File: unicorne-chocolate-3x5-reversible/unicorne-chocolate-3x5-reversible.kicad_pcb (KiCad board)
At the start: 2 copper layers, 114.7 x 91.4 mm, 84 parts, among them J1 MJ-4PP-9, J2 Conn_01x05, J3 Conn_01x02, J4 Conn_01x03, SW1 SW_CHOC_HS, SW10 SW_CHOC_HS, SW11 SW_CHOC_HS, SW12 SW_CHOC_HS, SW13 SW_CHOC_HS, SW14 SW_CHOC_HS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

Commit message: amend PCB
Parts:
- renumbered Left to R1, Right to R2
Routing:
- net col2: track 184.8 -> 190.9 mm
- net Net-(L22-DOUT): track 61.4 -> 63.2 mm
- net Net-(D12-A): track 13.0 -> 14.5 mm
- net VCC: track 524.0 -> 522.7 mm
- net GND: vias 18 -> 20

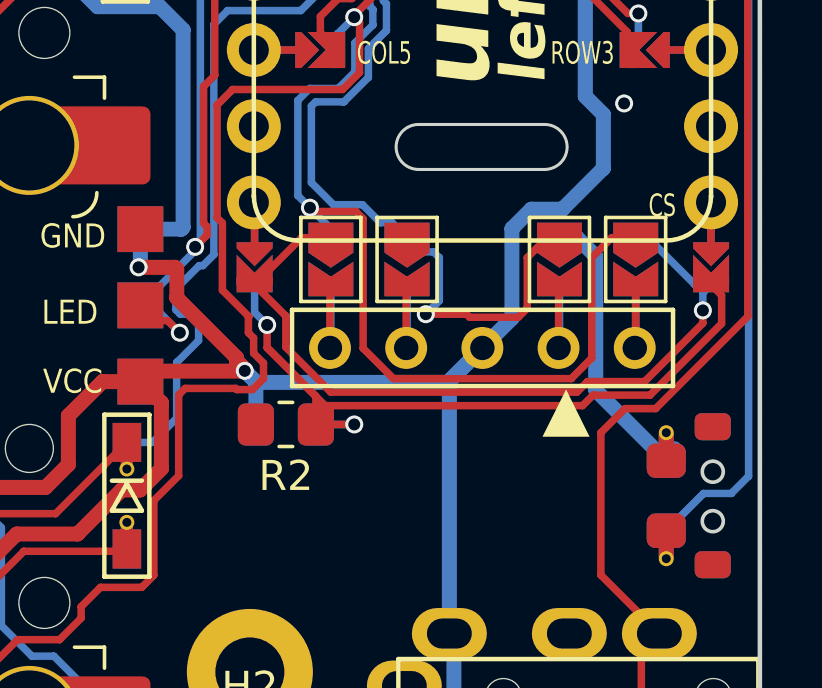
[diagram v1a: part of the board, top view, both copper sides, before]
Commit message: amend silkscreen
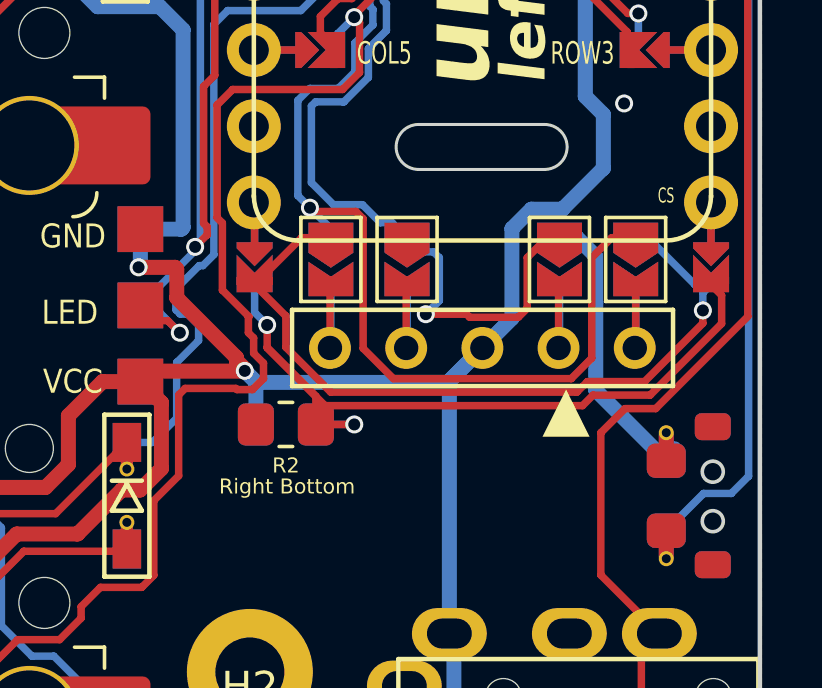
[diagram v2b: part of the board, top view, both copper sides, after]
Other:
- board text added: "Left Bottom"
- board text added: "Right Bottom"
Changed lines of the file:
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@@
         (effects (font (size 0.75 0.5) (thickness 0.125)) (justify mirror))
     )
-    (fp_text user "CS" (at -5.8674 13.9947) (layer "B.SilkS")
-        (effects (font (size 0.75 0.5) (thickness 0.125)) (justify mirror))
+    (fp_text user "CS" (at -6.22 13.64) (layer "B.SilkS")
+        (effects (font (size 0.5 0.3) (thickness 0.075)) (justify mirror))
     )
     (fp_text user "SDA" (at -3.45 -3.8488) (layer "B.SilkS")
@@
         (effects (font (size 0.75 0.5) (thickness 0.125)))
     )
-    (fp_text user "CS" (at 6.1468 14.0255) (layer "F.SilkS")
-        (effects (font (size 0.75 0.5) (thickness 0.125)))
+    (fp_text user "CS" (at 6.2724 13.6892) (layer "F.SilkS")
+        (effects (font (size 0.5 0.3) (thickness 0.075)))
     )
     (fp_text user "LED" (at 3.7595 -13.978) (layer "F.SilkS")
@@
     (property "ki_keywords" "R res resistor")
     (attr smd)
-    (fp_text reference "R2" (at 0 1.72) (layer "F.SilkS")
-        (effects (font (size 1 1) (thickness 0.15)))
+    (fp_text reference "R2" (at 0 1.37) (layer "F.SilkS")
+        (effects (font (size 0.5 0.5) (thickness 0.075)))
     )
     (fp_text value "10k" (at 0 1.65) (layer "F.Fab")
@@
     (property "ki_keywords" "R res resistor")
     (attr smd)
-    (fp_text reference "R1" (at 0.01 1.72) (layer "B.SilkS")
-        (effects (font (size 1 1) (thickness 0.15)) (justify mirror))
+    (fp_text reference "R1" (at 0.01 1.37) (layer "B.SilkS")
+        (effects (font (size 0.5 0.5) (thickness 0.075) bold) (justify mirror))
     )
     (fp_text value "10k" (at 0 -1.65) (layer "B.Fab")
@@
     (fp_line (start 9.104 -2.775) (end 7.504 -2.775)
       (stroke (width 0.05) (type solid)) (layer "B.CrtYd"))
-    (fp_arc (start 0.299999 -3.624999) (mid 1.577272 -3.167235) (end 2.455444 -2.13293)
+    (fp_arc (start 0.299999 -3.624999) (mid 1.577271 -3.167235) (end 2.455444 -2.13293)
       (stroke (width 0.05) (type solid)) (layer "B.CrtYd"))
     (fp_arc (start 3.4 -1.475) (mid 2.826424 -1.655848) (end 2.460307 -2.13298)
@@
     (effects (font (size 1 1) (thickness 0.125)) (justify left mirror))
   )
+  (gr_text "Left Bottom" (at 180.92 109.69) (layer "B.SilkS")
+    (effects (font (size 0.5 0.5) (thickness 0.075)) (justify left mirror))
+  )
   (gr_text "GND" (at 171.8 106.172) (layer "B.SilkS")
     (effects (font (size 0.8 0.7) (thickness 0.125)) (justify mirror))
@@
     )
   )
+  (gr_text "Right Bottom" (at 176.67 109.67) (layer "F.SilkS")
+    (effects (font (size 0.5 0.5) (thickness 0.075)) (justify left))
+  )
   (gr_text "▲" (at 189.03 107.94) (layer "F.SilkS")

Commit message: small tweak
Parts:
- added JP9: Jumper_3_Bridged12, TB2086_MISC:SolderJumper-3_P1.3mm_Bridged2Bar12_RoundedPad1.0x1.5mm_rev, F.Cu at (188.6, 110.2)
- added R3: 4.7k, TB2086_SMD:R_0805_2012Metric_Pad1.20x1.40mm_HandSolder_rev, F.Cu at (185.1, 109.3)
- added R4: 4.7k, TB2086_SMD:R_0805_2012Metric_Pad1.20x1.40mm_HandSolder_rev, F.Cu at (185.1, 111.2)
- D1, D10, D11, D12, D13, D14, D15, D16, D17, D18, D2, D3, D4, D5, D6, D7, D8, D9: footprint KBD_PARTS:D3_SMD_rev -> TB2086_SMD:D3_SMD_rev
- H1, H2: footprint KBD_PARTS:M2_Hole_TH -> TB2086_MISC:M2_Hole_TH
- H3, H4, H5, H6, H7: footprint KBD_PARTS:M2_Hole_TH_Outside -> TB2086_MISC:M2_Hole_TH_Outside
- J1: footprint KBD_PARTS:TRRS-PJ-320A-rev -> TB2086_MISC:TRRS-PJ-320A-rev
- J2: footprint KBD_PARTS:Nice!View -> TB2086_MISC:Nice!View
- J3: footprint KBD_PARTS:Molex_Pico-EZmate_78171-0002_1x02-1MP_P1.20mm_Vertical_rev -> TB2086_SMD:Molex_Pico-EZmate_78171-0002_1x02-1MP_P1.20mm_Vertical_rev
- J4: footprint KBD_PARTS:StripLED_rev -> TB2086_MISC:StripLED_rev
- L1, L10, L11, L12, L13, L14, L15, L16, L17, L18, L2, L3, L4, L5, L6, L7, L8, L9: value SK6812MINI_back -> SK6812MINI-E; footprint KBD_PARTS:LED_SK6812MINI_PLCC4_3.5x3.5mm_P1.75mm_back_rev -> TB2086_LED:LED_SK6812MINI-E_rev
- L19, L20, L21, L22, L23, L24: footprint KBD_PARTS:LED_SK6812MINI_PLCC4_3.5x3.5mm_P1.75mm_rev -> TB2086_LED:LED_SK6812MINI_PLCC4_3.5x3.5mm_P1.75mm_rev_all
- PSW1: footprint Akizukidenshi:SW_SPDT_PCM12_reversible -> TB2086_SMD:SW_SPDT_PCM12_reversible
- RSW1: footprint KBD_PARTS:SMT 2X4X3.5MM Tactile Tact Push Button -> TB2086_SMD:SMT 2X4X3.5MM Tactile Tact Push Button rev
- SW1, SW10, SW11, SW12, SW13, SW14, SW15, SW16, SW17, SW2, SW3, SW4, SW5, SW6, SW7, SW8, SW9: footprint KBD_PARTS:SW_choc_v1_v2_HS_1u_reversible -> TB2086_KEYSWITCH:SW_choc_v1_v2_HS_1u_reversible
- SW18: footprint KBD_PARTS:SW_choc_v1_v2_HS_1.5u_reversible -> TB2086_KEYSWITCH:SW_choc_v1_v2_HS_1.5u_reversible
- U1: footprint KBD_PARTS:ProMicro-ish-rev-unrouted_3x5 -> TB2086_MISC:ProMicro-ish-dn-rev-unrouted_3x5
- moved H6 0.13 mm to (98.5, 105.8)
- moved H7 0.13 mm to (98.5, 86.8)
- turned L13 to 180 degrees
- turned L15 to 180 degrees
- turned L19 to 0 degrees
- turned L2 to 180 degrees
- turned L22 to 0 degrees
- turned L23 to 0 degrees
- turned L24 to 0 degrees
- turned L3 to 180 degrees
- turned L7 to 0 degrees
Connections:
- J1 pad A: unconnected-(J1-PadA) -> SCL
- J1 pad B: DATA -> Net-(JP9-C)
- L1 pad 1: unconnected-(L1-DOUT-Pad1) -> VCC
- L1 pad 2: GND -> unconnected-(L1-DOUT-Pad2)
- L1 pad 3: Net-(L1-DIN) -> GND
- L1 pad 4: VCC -> Net-(L1-DIN)
- L10 pad 1: Net-(L10-DOUT) -> VCC
- L10 pad 2: GND -> Net-(L10-DOUT)
- L10 pad 3: Net-(L10-DIN) -> GND
- L10 pad 4: VCC -> Net-(L10-DIN)
- L11 pad 1: Net-(L11-DOUT) -> VCC
- L11 pad 2: GND -> Net-(L11-DOUT)
- L11 pad 3: Net-(L11-DIN) -> GND
- L11 pad 4: VCC -> Net-(L11-DIN)
- L12 pad 1: Net-(L11-DIN) -> VCC
- L12 pad 2: GND -> Net-(L11-DIN)
- L12 pad 3: Net-(L12-DIN) -> GND
- L12 pad 4: VCC -> Net-(L12-DIN)
- L13 pad 1: Net-(L13-DOUT) -> VCC
- L13 pad 2: GND -> Net-(L13-DOUT)
- L13 pad 3: Net-(L13-DIN) -> GND
- L13 pad 4: VCC -> Net-(L13-DIN)
- L14 pad 1: Net-(L14-DOUT) -> VCC
- L14 pad 2: GND -> Net-(L14-DOUT)
- L14 pad 3: Net-(L14-DIN) -> GND
- L14 pad 4: VCC -> Net-(L14-DIN)
- L15 pad 1: Net-(L10-DIN) -> VCC
- L15 pad 2: GND -> Net-(L10-DIN)
- L15 pad 3: Net-(L15-DIN) -> GND
- L15 pad 4: VCC -> Net-(L15-DIN)
- L16 pad 1: Net-(L13-DIN) -> VCC
- L16 pad 2: GND -> Net-(L13-DIN)
- L16 pad 3: Net-(L16-DIN) -> GND
- L16 pad 4: VCC -> Net-(L16-DIN)
- L17 pad 1: Net-(L16-DIN) -> VCC
- L17 pad 2: GND -> Net-(L16-DIN)
- L17 pad 3: Net-(L14-DOUT) -> GND
- L17 pad 4: VCC -> Net-(L14-DOUT)
- L18 pad 1: Net-(L15-DIN) -> VCC
- L18 pad 2: GND -> Net-(L15-DIN)
- L18 pad 3: Net-(L18-DIN) -> GND
- L18 pad 4: VCC -> Net-(L18-DIN)
- L2 pad 1: Net-(L2-DOUT) -> VCC
- L2 pad 2: GND -> Net-(L2-DOUT)
- L2 pad 3: Net-(L2-DIN) -> GND
- L2 pad 4: VCC -> Net-(L2-DIN)
- L3 pad 1: Net-(L2-DIN) -> VCC
- L3 pad 2: GND -> Net-(L2-DIN)
- L3 pad 3: Net-(L3-DIN) -> GND
- L3 pad 4: VCC -> Net-(L3-DIN)
- L4 pad 1: Net-(L4-DOUT) -> VCC
- L4 pad 2: GND -> Net-(L4-DOUT)
- L4 pad 3: Net-(L4-DIN) -> GND
- L4 pad 4: VCC -> Net-(L4-DIN)
- L5 pad 1: Net-(L4-DIN) -> VCC
- L5 pad 2: GND -> Net-(L4-DIN)
- L5 pad 3: Net-(L10-DOUT) -> GND
- L5 pad 4: VCC -> Net-(L10-DOUT)
- L6 pad 1: Net-(L1-DIN) -> VCC
- L6 pad 2: GND -> Net-(L1-DIN)
- L6 pad 3: Net-(L11-DOUT) -> GND
- L6 pad 4: VCC -> Net-(L11-DOUT)
- L7 pad 1: Net-(L12-DIN) -> VCC
- L7 pad 2: GND -> Net-(L12-DIN)
- L7 pad 3: Net-(L2-DOUT) -> GND
- L7 pad 4: VCC -> Net-(L2-DOUT)
- L8 pad 1: Net-(L3-DIN) -> VCC
- L8 pad 2: GND -> Net-(L3-DIN)
- L8 pad 3: Net-(L13-DOUT) -> GND
- L8 pad 4: VCC -> Net-(L13-DOUT)
- L9 pad 1: Net-(L14-DIN) -> VCC
- L9 pad 2: GND -> Net-(L14-DIN)
- L9 pad 3: Net-(L4-DOUT) -> GND
- L9 pad 4: VCC -> Net-(L4-DOUT)
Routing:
- net Net-(L2-DIN): track 22.2 -> 61.9 mm, vias 2 -> 0
- net Net-(L3-DIN): track 23.7 -> 48.0 mm, vias 0 -> 2
- net row0: track 125.2 -> 147.8 mm
- net SCL: track 40.6 -> 59.4 mm, vias 2 -> 4
- net GND: track 61.8 -> 45.4 mm, vias 20 -> 23
- net Net-(JP9-C): track 0.00 -> 16.3 mm
- net LED: track 76.6 -> 61.5 mm
- net Net-(L10-DOUT): track 23.4 -> 38.4 mm
- net Net-(L23-DOUT): track 59.6 -> 45.0 mm, vias 0 -> 1
- net Net-(L22-DOUT): track 63.2 -> 52.0 mm
- net SDA: track 61.7 -> 72.7 mm, vias 2 -> 4
- net DATA: track 75.2 -> 64.2 mm, vias 1 -> 2
- net Net-(D15-A): track 25.4 -> 14.8 mm
- net Net-(L10-DIN): track 24.4 -> 33.7 mm
- net Net-(L13-DOUT): track 36.1 -> 27.5 mm, vias 1 -> 0
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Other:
- outline, holes or cut-outs redrawn
- board text added: "left hand"
- board text added: "right hand"
- board text removed: "left"
- board text removed: "right"
